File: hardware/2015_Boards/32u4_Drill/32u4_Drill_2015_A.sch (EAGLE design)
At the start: 26 parts, among them U2 XBEE-1B3

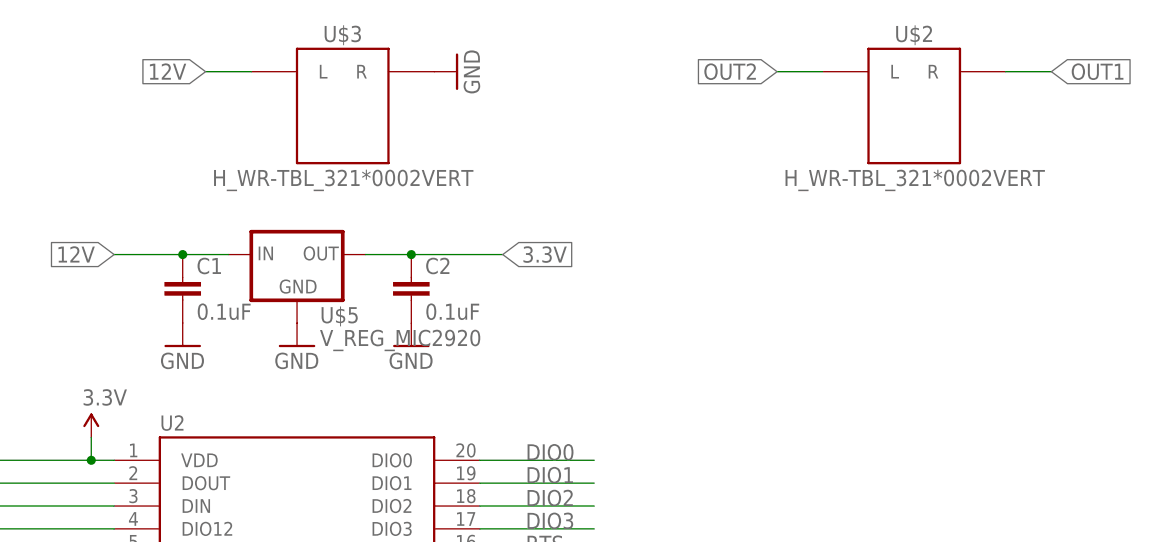
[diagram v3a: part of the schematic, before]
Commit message: Updated values in Schematic. Makes BOM easier
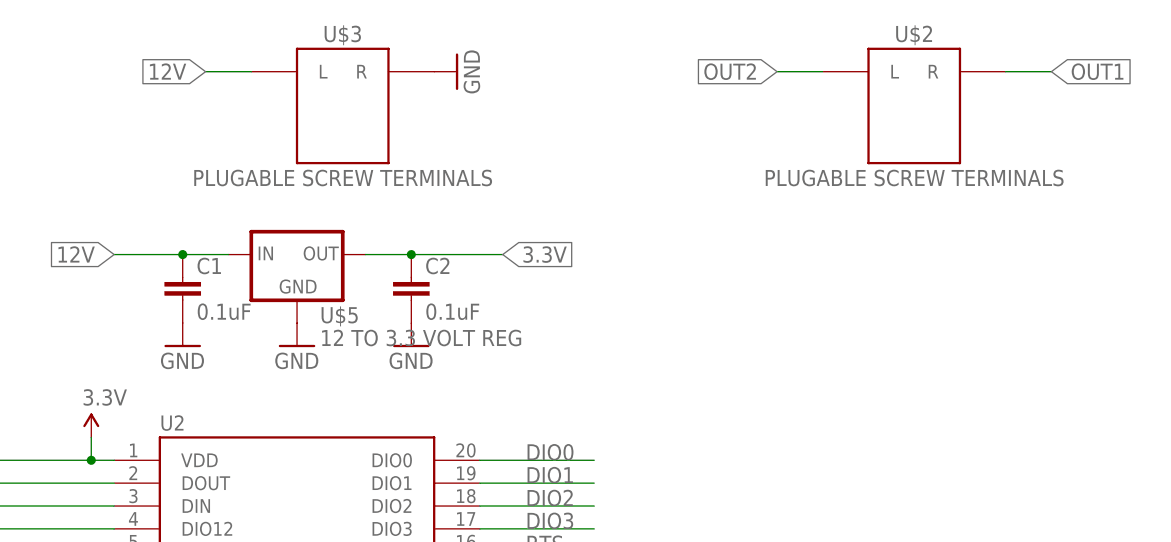
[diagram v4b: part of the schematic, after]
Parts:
- U$2, U$3: value H_WR-TBL_321*0002VERT -> PLUGABLE SCREW TERMINALS
- U$5: value V_REG_MIC2920 -> 12 TO 3.3 VOLT REG
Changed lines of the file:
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@@
 <part name="P+3" library="SparkFun" deviceset="3.3V" device=""/>
 <part name="P+4" library="SparkFun" deviceset="3.3V" device=""/>
-<part name="U$3" library="MRDT-2015-PowerBoard" deviceset="H_WR-TBL_32*1*0002" device="VERT" value="H_WR-TBL_321*0002VERT"/>
-<part name="U$5" library="SparkFun-PowerIC" deviceset="V_REG_MIC2920" device=""/>
+<part name="U$3" library="MRDT-2015-PowerBoard" deviceset="H_WR-TBL_32*1*0002" device="VERT" value="PLUGABLE SCREW TERMINALS"/>
+<part name="U$5" library="SparkFun-PowerIC" deviceset="V_REG_MIC2920" device="" value="12 TO 3.3 VOLT REG"/>
 <part name="GND4" library="SparkFun" deviceset="GND" device=""/>
 <part name="GND9" library="SparkFun" deviceset="GND" device=""/>
@@
 <part name="GND7" library="SparkFun" deviceset="GND" device=""/>
 <part name="GND8" library="SparkFun" deviceset="GND" device=""/>
-<part name="U$2" library="MRDT-2015-PowerBoard" deviceset="H_WR-TBL_32*1*0002" device="VERT" value="H_WR-TBL_321*0002VERT"/>
+<part name="U$2" library="MRDT-2015-PowerBoard" deviceset="H_WR-TBL_32*1*0002" device="VERT" value="PLUGABLE SCREW TERMINALS"/>
 <part name="U$4" library="MRDT-2015-General" deviceset="BTM7752G" device=""/>
 <part name="GND10" library="SparkFun" deviceset="GND" device=""/>

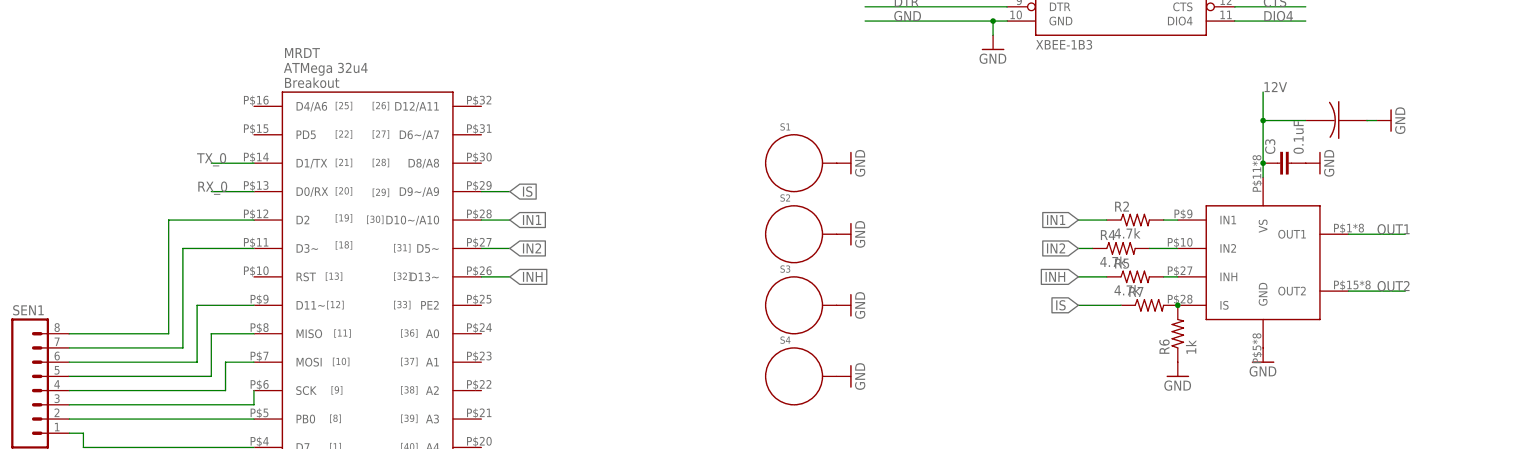
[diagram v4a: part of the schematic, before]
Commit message: Fixed a schematic connection issue
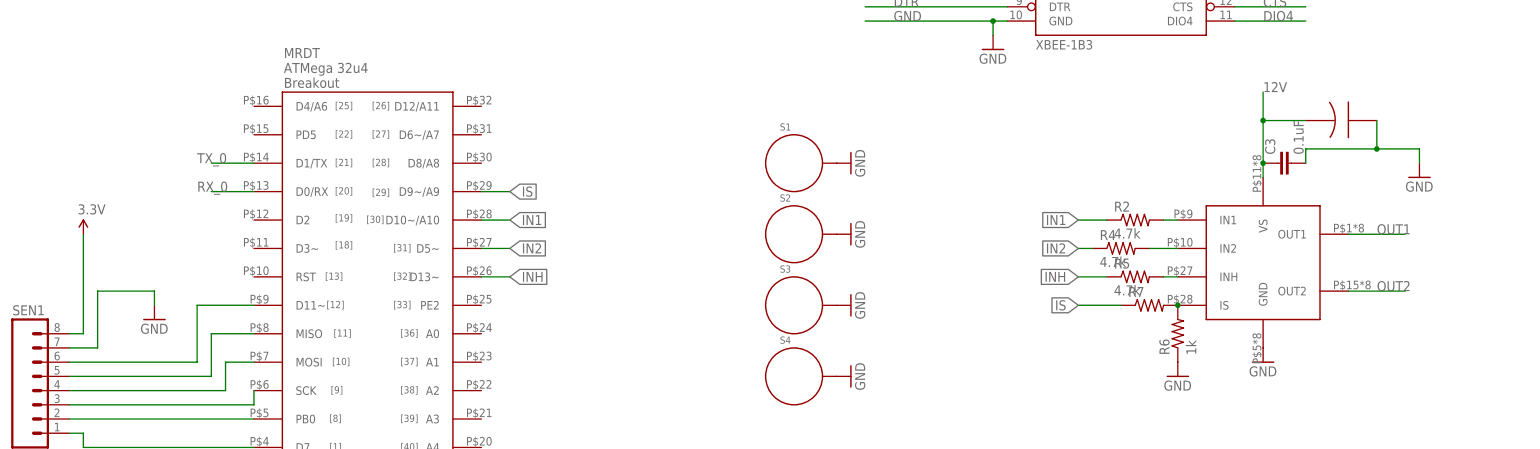
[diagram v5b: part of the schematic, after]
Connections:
- removed net N$13: SEN1.7, U$1.D3~
- net 3.3V: now also SEN1.8
- net GND: now also U$6.NEG
- net N$14: now also SEN1.7; no longer SEN1.8, U$1.D2
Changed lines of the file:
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@@
 <part name="R7" library="SparkFun-Passives" deviceset="RESISTOR" device="1206"/>
 <part name="C3" library="SparkFun-Passives" deviceset="CAP" device="1206" value="0.1uF"/>
-<part name="GND14" library="SparkFun" deviceset="GND" device=""/>
-<part name="GND15" library="SparkFun" deviceset="GND" device=""/>
+<part name="SEN1" library="SparkFun-Connectors" deviceset="M08" device="1X08"/>
+<part name="SUPPLY1" library="SparkFun-Aesthetics" deviceset="3.3V" device=""/>
+<part name="GND16" library="SparkFun-Aesthetics" deviceset="GND" device=""/>
 <part name="U$6" library="New" deviceset="100UF-ELECTRO-CAP" device=""/>
-<part name="SEN1" library="SparkFun-Connectors" deviceset="M08" device="1X08"/>
+<part name="GND14" library="SparkFun-Aesthetics" deviceset="GND" device=""/>
 </parts>
 <sheets>
@@
 <instance part="R7" gate="G$1" x="165.1" y="45.72"/>
 <instance part="C3" gate="G$1" x="190.5" y="71.12" rot="R90"/>
-<instance part="GND14" gate="1" x="208.28" y="78.74" rot="R90"/>
-<instance part="GND15" gate="1" x="195.58" y="71.12" rot="R90"/>
-<instance part="U$6" gate="G$1" x="220.98" y="66.04"/>
 <instance part="SEN1" gate="G$1" x="-33.02" y="30.48"/>
+<instance part="SUPPLY1" gate="G$1" x="-25.4" y="58.42"/>
+<instance part="GND16" gate="1" x="-12.7" y="43.18"/>
+<instance part="U$6" gate="G$1" x="198.12" y="78.74"/>
+<instance part="GND14" gate="1" x="213.36" y="68.58"/>
 </instances>
 <busses>
@@
 <segment>
 <pinref part="C3" gate="G$1" pin="2"/>
-<pinref part="GND15" gate="1" pin="GND"/>
-</segment>
-<segment>
+<wire x1="213.36" y1="73.66" x2="205.74" y2="73.66" width="0.1524" layer="91"/>
+<wire x1="205.74" y1="73.66" x2="193.04" y2="73.66" width="0.1524" layer="91"/>
+<wire x1="193.04" y1="73.66" x2="193.04" y2="71.12" width="0.1524" layer="91"/>
+<wire x1="213.36" y1="73.66" x2="213.36" y2="71.12" width="0.1524" layer="91"/>
+<pinref part="U$6" gate="G$1" pin="NEG"/>
+<wire x1="205.74" y1="78.74" x2="205.74" y2="73.66" width="0.1524" layer="91"/>
+<junction x="205.74" y="73.66"/>
 <pinref part="GND14" gate="1" pin="GND"/>
-<wire x1="205.74" y1="78.74" x2="203.962" y2="78.74" width="0.1524" layer="91"/>
 </segment>
 </net>
@@
 <junction x="172.72" y="142.24"/>
 </segment>
+<segment>
+<pinref part="SEN1" gate="G$1" pin="8"/>
+<wire x1="-27.94" y1="40.64" x2="-25.4" y2="40.64" width="0.1524" layer="91"/>
+<wire x1="-25.4" y1="40.64" x2="-25.4" y2="58.42" width="0.1524" layer="91"/>
+<pinref part="SUPPLY1" gate="G$1" pin="3.3V"/>
+</segment>
 </net>
 <net name="DIO4" class="0">
@@
 <wire x1="185.42" y1="71.12" x2="185.42" y2="78.74" width="0.1524" layer="91"/>
 <junction x="185.42" y="71.12"/>
-<pinref part="U$6" gate="G$1" pin="POS"/>
 <wire x1="185.42" y1="78.74" x2="185.42" y2="83.82" width="0.1524" layer="91"/>
 <wire x1="193.04" y1="78.74" x2="185.42" y2="78.74" width="0.1524" layer="91"/>
 <junction x="185.42" y="78.74"/>
+<pinref part="U$6" gate="G$1" pin="POS"/>
 </segment>
 </net>
@@
 </segment>
 </net>
-<net name="N$13" class="0">
-<segment>
-<pinref part="U$1" gate="G$1" pin="D3~"/>
-<wire x1="5.08" y1="55.88" x2="-7.62" y2="55.88" width="0.1524" layer="91"/>
+<net name="N$14" class="0">
+<segment>
 <pinref part="SEN1" gate="G$1" pin="7"/>
-<wire x1="-7.62" y1="55.88" x2="-7.62" y2="38.1" width="0.1524" layer="91"/>
-<wire x1="-7.62" y1="38.1" x2="-27.94" y2="38.1" width="0.1524" layer="91"/>
-</segment>
-</net>
-<net name="N$14" class="0">
-<segment>
-<pinref part="U$1" gate="G$1" pin="D2"/>
-<wire x1="5.08" y1="60.96" x2="-10.16" y2="60.96" width="0.1524" layer="91"/>
-<pinref part="SEN1" gate="G$1" pin="8"/>
-<wire x1="-10.16" y1="60.96" x2="-10.16" y2="40.64" width="0.1524" layer="91"/>
-<wire x1="-10.16" y1="40.64" x2="-27.94" y2="40.64" width="0.1524" layer="91"/>
-</segment>
-</net>
+<wire x1="-27.94" y1="38.1" x2="-22.86" y2="38.1" width="0.1524" layer="91"/>
+<wire x1="-22.86" y1="38.1" x2="-22.86" y2="48.26" width="0.1524" layer="91"/>
+<wire x1="-22.86" y1="48.26" x2="-12.7" y2="48.26" width="0.1524" layer="91"/>
+<wire x1="-12.7" y1="48.26" x2="-12.7" y2="45.72" width="0.1524" layer="91"/>
+<pinref part="GND16" gate="1" pin="GND"/>
+</segment>
+</net>
